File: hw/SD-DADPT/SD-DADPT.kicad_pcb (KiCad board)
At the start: 2 copper layers, 85.1 x 72.4 mm, 16 parts, among them J1 CONN 1x8 Socket, J2 CONN 1x8 Socket, J3 CONN 1x6 Socket, J4 CONN 1x6 Socket, J5 CONN 1x22 SOCKET, J6 HDR 2x10 Pin, J7 CONN 1x6 HDR, J8 Screw_Terminal_01x02

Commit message: ZMB: v1.0 Board RFP
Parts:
- added H5: MountingHole, MountingHole:MountingHole_3.2mm_M3, F.Cu at (72.6, 118.6)
- C3, J8: moved to B.Cu
- moved C2 0.76 mm to (122.5, 81.3)
- moved J3 0.76 mm to (112.5, 77.5)
- moved J4 0.76 mm to (130.3, 77.5)
- moved J8 0.59 mm to (79.6, 138.2)
- moved H1 0.44 mm to (73.4, 138.7)
- moved H4 0.44 mm to (149.6, 138.7)
- moved H2 0.44 mm to (73.4, 75.2)
- moved H3 0.44 mm to (149.6, 75.2)
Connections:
- J1 pad 1: /D0 -> unconnected-(J1-Pin_1-Pad1)
- J1 pad 2: /D1 -> unconnected-(J1-Pin_2-Pad2)
- J1 pad 3: /SPI_SEL- -> /SPI_CLK
- J1 pad 4: /SPI_MOSI -> /SPI_MISO
- J1 pad 5: /SPI_MISO -> /SPI_MOSI
- J1 pad 6: /SPI_CLK -> /SPI_SEL-
- J1 pad 7: unconnected-(J1-Pin_7-Pad7) -> /D1
- J1 pad 8: unconnected-(J1-Pin_8-Pad8) -> /D0
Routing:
- net /SPI_SEL-: track 19.1 -> 26.8 mm
- net /SPI_CLK: track 25.5 -> 21.0 mm
- net /SPI_MISO: track 23.6 -> 19.6 mm
- net /D0: track 45.1 -> 41.8 mm
- net /BLPWR: track 13.8 -> 16.4 mm
- net /SPI_MOSI: track 21.6 -> 23.2 mm
- net /WR-: track 96.0 -> 97.1 mm
- net /RESET-: track 83.1 -> 84.2 mm
- net GND: track 24.8 -> 25.7 mm, vias 7 -> 10
- net /D1: track 33.9 -> 34.8 mm
- net /RD-: track 93.6 -> 94.4 mm

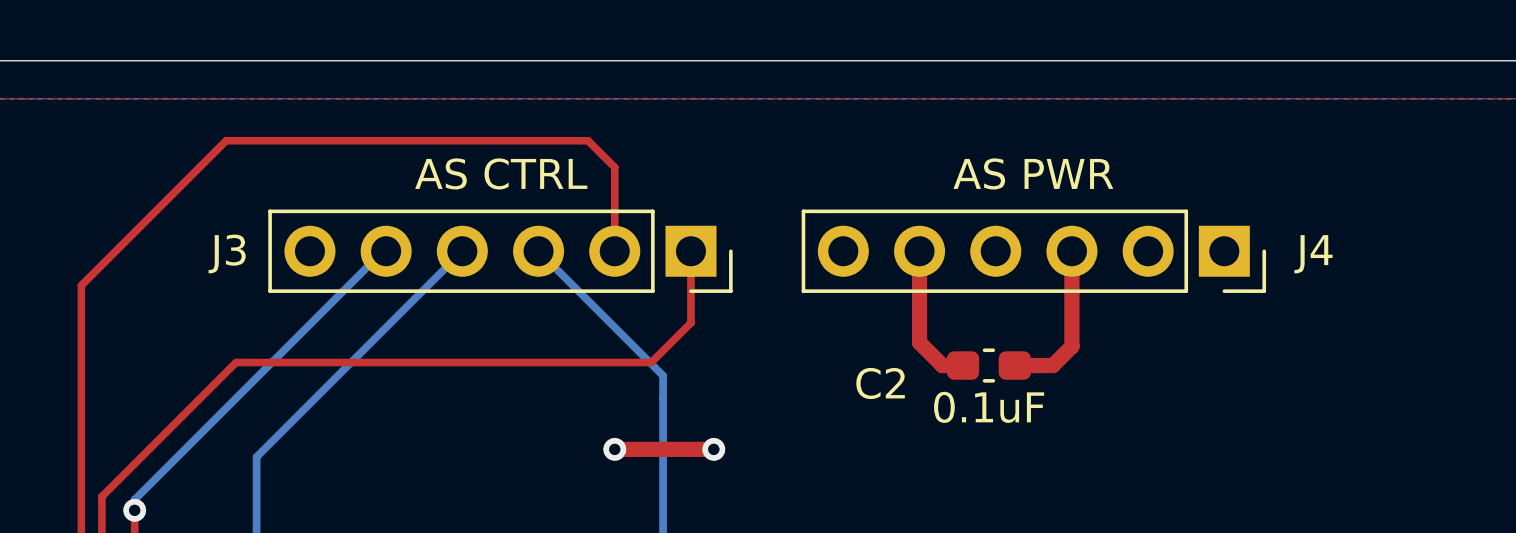
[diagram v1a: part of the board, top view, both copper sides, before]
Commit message: ZMB gerbers created. OLED display portion updates.
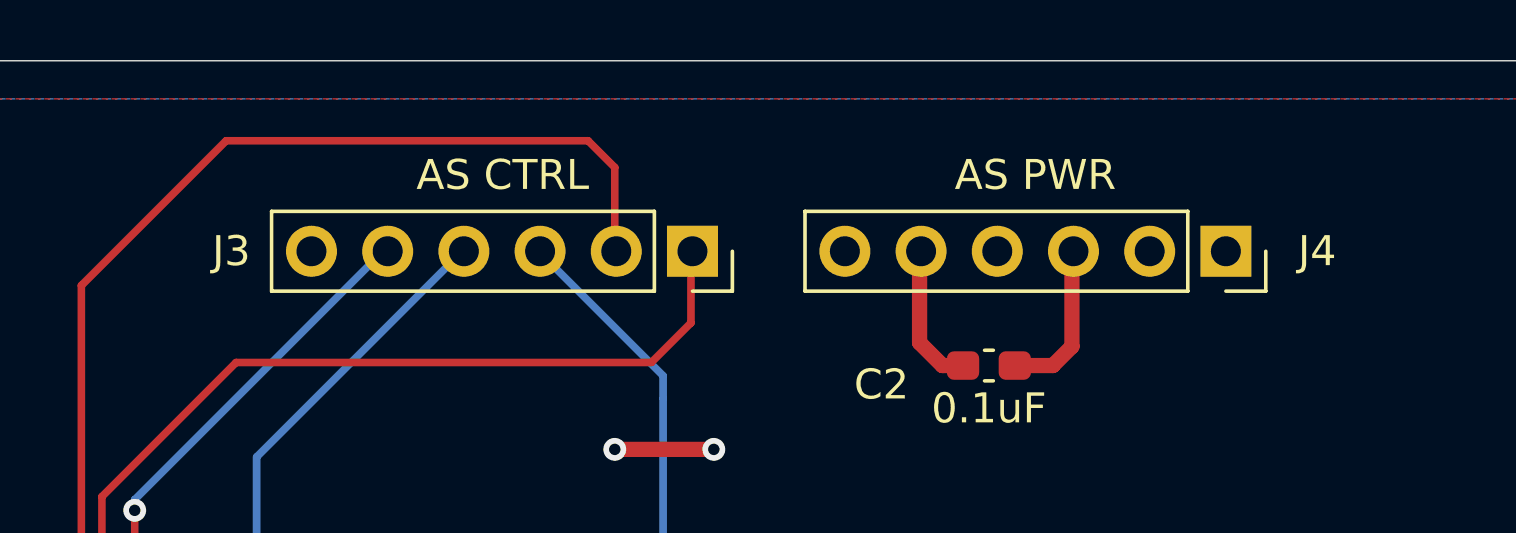
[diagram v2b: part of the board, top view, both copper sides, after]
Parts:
- moved J4 0.05 mm to (130.4, 77.5)
- moved J3 0.05 mm to (112.6, 77.5)
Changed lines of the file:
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@@
 	(title_block
 		(title "Display Adapter & Cable Board")
-		(date "2025-11-02")
-		(rev "PR-1.0")
+		(date "2025-11-24")
+		(rev "PR-1.0b")
 		(company "SilkyDESIGN")
 		(comment 1 "Copyright 2025 AESilky")
@@
 		(locked yes)
 		(layer "F.Cu")
-		(at 112.522 77.47 -90)
+		(at 112.5728 77.47 -90)
 		(descr "Through hole straight socket strip, 1x06, 2.54mm pitch, single row (from Kicad 4.0.7), script generated")
 		(tags "Through hole socket strip THT 1x06 2.54mm single row")
@@
 		(locked yes)
 		(layer "F.Cu")
-		(at 130.302 77.47 -90)
+		(at 130.3528 77.47 -90)
 		(descr "Through hole straight socket strip, 1x06, 2.54mm pitch, single row (from Kicad 4.0.7), script generated")
 		(tags "Through hole socket strip THT 1x06 2.54mm single row")
